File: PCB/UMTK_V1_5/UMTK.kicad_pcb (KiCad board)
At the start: 4 copper layers, 88 parts, among them J1 Motor Out, J2 ESTOP, J3 JST 4pin, J5 PJ-102BH, J8 10033526-N3212LF, Q1 Q_PNP_BEC, U1 DRV8873SPWPRQ1, U10 LM2576HVS-5, U11 SN74LVC1T45DCK, U12 SN74LVC1T45DCK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

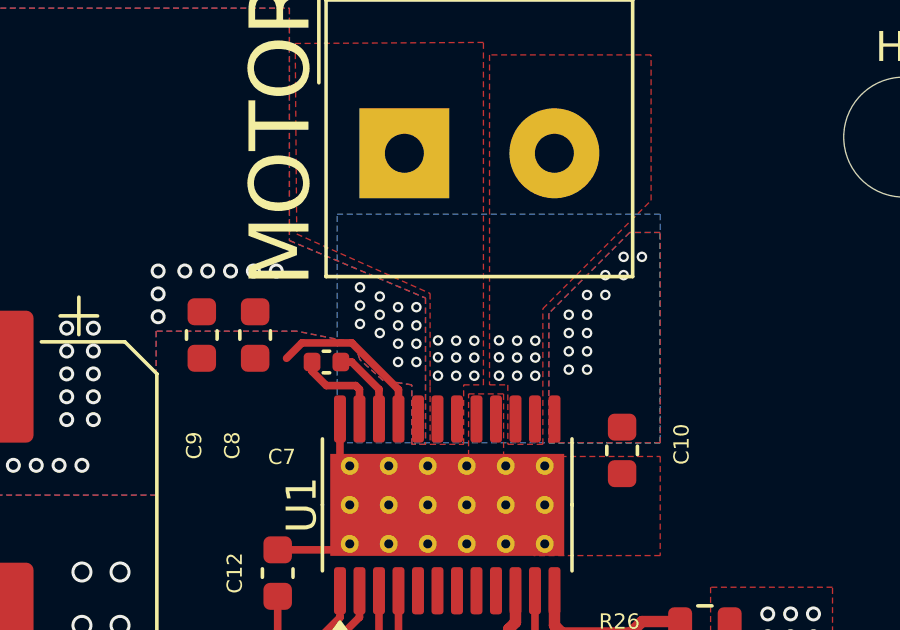
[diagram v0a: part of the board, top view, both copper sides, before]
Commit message: Update Via sizes to 0.3 / 0.45
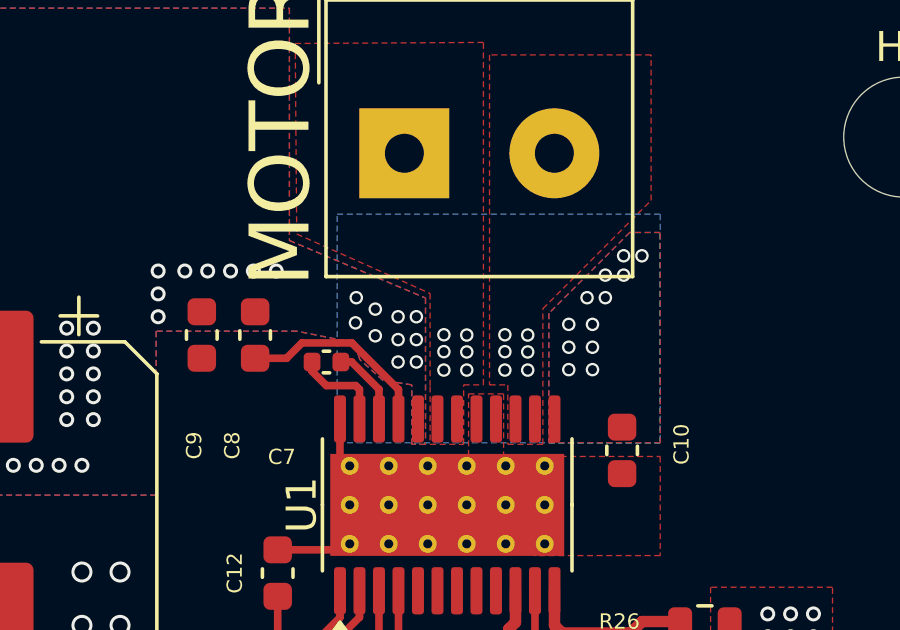
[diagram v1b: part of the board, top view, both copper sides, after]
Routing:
- net Net-(U1-VCP): track 5.57 -> 6.62 mm
- net VMOTOR: vias 80 -> 74
- net /MotorDriver/VM-: vias 9 -> 6
- net /MotorDriver/VM+: vias 9 -> 6

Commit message: Routing
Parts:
- added H9: MountingHole, MountingHole:MountingHole_4mm, F.Cu at (160.0, 25.0)
- J1, J2: footprint TerminalBlock_Altech:Altech_AK100_1x02_P5.00mm -> Connector_Phoenix_MC_HighVoltage:PhoenixContact_MC_1,5_2-G-5.08_1x02_P5.08mm_Horizontal
- J3: value JST 4pin -> LOADCELL; footprint Connector_JST:JST_XH_B4B-XH-A_1x04_P2.50mm_Vertical -> Connector_Phoenix_MC:PhoenixContact_MC_1,5_4-G-3.81_1x04_P3.81mm_Horizontal
- moved J3 8.70 mm to (97.7, 25.9), turned to 180 degrees
- moved J1 8.63 mm to (177.0, 25.6), turned to 180 degrees
- moved H7 5.39 mm to (170.0, 72.0)
- moved H8 5.39 mm to (135.0, 72.0)
- moved J2 4.87 mm to (148.3, 25.5), turned to 180 degrees
- moved JP2 4.45 mm to (121.8, 44.7)
- moved JP3 3.43 mm to (121.8, 49.1)
- moved C10 3.36 mm to (179.0, 35.4)
- moved C7 3.36 mm to (169.1, 32.5)
- moved C8 3.36 mm to (166.7, 31.6)
- moved U1 3.36 mm to (173.1, 37.3)
- moved C12 3.36 mm to (167.5, 39.5)
- moved C9 3.36 mm to (165.0, 31.6)
- moved R26 3.36 mm to (181.7, 41.1)
- moved R27 3.36 mm to (181.7, 43.0)
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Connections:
- J1 pad 1: /MotorDriver/VM+ -> /MotorDriver/VM-
- J1 pad 2: /MotorDriver/VM- -> /MotorDriver/VM+
- J2 pad 1: +12V -> VMOTOR
- J2 pad 2: VMOTOR -> +12V
- J3 pad 2: /HX711/LCS- -> /HX711/LCS+
- J3 pad 3: /HX711/LCS+ -> /HX711/LCS-
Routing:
- net +5V: track 25.6 -> 268.7 mm, vias 22 -> 48
- net /Arduino/MOT_DISABLE: track 0.00 -> 177.6 mm, vias 0 -> 3
- net /Arduino/MOT_nOL: track 0.00 -> 169.8 mm, vias 0 -> 2
- net /Arduino/MOT_nITRIP: track 0.00 -> 169.0 mm, vias 0 -> 2
- net /Arduino/MOT_PH_IN2: track 0.00 -> 164.1 mm, vias 0 -> 4
- net /Arduino/MOT_EN_N1: track 0.00 -> 161.4 mm, vias 0 -> 1
- net /Arduino/MOT_SENSE2: track 5.61 -> 146.8 mm, vias 0 -> 2
- net /Arduino/MOT_SENSE1: track 8.35 -> 134.7 mm, vias 0 -> 2
- net /Arduino/SLIDE_DAT_DIR: track 10.1 -> 123.6 mm, vias 0 -> 2
- net /Arduino/SLIDE_DAT: track 0.00 -> 106.2 mm, vias 0 -> 2
- net /Arduino/SLIDE_CLK_DIR: track 12.3 -> 111.6 mm, vias 0 -> 2
- net /Arduino/SLIDE_CLK: track 0.00 -> 92.8 mm, vias 0 -> 2
- net /Arduino/SW_1: track 10.2 -> 92.2 mm, vias 1 -> 2
- net /Arduino/SW_5: track 66.3 -> 1.90 mm
- net /Arduino/LC_SCK: track 0.00 -> 54.9 mm, vias 0 -> 1
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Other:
- board text added: "3v3 CUT & Solder"
- board text removed: "3v3 (CUT & Solder)"

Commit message: Dumbass has push and shove routing off
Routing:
- net /Arduino/SW_2: track 0.00 -> 97.4 mm, vias 0 -> 4
- net +5V: track 268.7 -> 265.6 mm
- net /Arduino/SW_5: track 1.90 -> 0.00 mm, vias 1 -> 0
- net /Arduino/SW_4: track 1.65 -> 0.00 mm, vias 1 -> 0
- net GND: track 60.3 -> 60.2 mm, vias 175 -> 174
- net Net-(U6-DIG_5): vias 4 -> 2
- net +12V: vias 42 -> 40

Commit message: Routing Done
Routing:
- net /Arduino/MOT_MODE: track 4.63 -> 158.5 mm, vias 0 -> 3
- net /Arduino/SW_5: track 0.00 -> 139.0 mm, vias 0 -> 4
- net /Arduino/SW_4: track 0.00 -> 132.6 mm, vias 0 -> 4
- net /Arduino/SW_3: track 0.00 -> 111.1 mm, vias 0 -> 3
- net /Arduino/LC_RATE: track 0.00 -> 72.9 mm, vias 0 -> 2
- net VDD: track 33.4 -> 82.4 mm, vias 19 -> 23
- net +5V: track 265.6 -> 310.8 mm, vias 48 -> 50
- net /Arduino/MOT_nITRIP: track 169.0 -> 182.8 mm
- net /Arduino/MOT_nOL: track 169.7 -> 183.3 mm
- net Net-(U4-B): track 0.00 -> 12.1 mm
- net GND: track 60.2 -> 70.5 mm, vias 174 -> 230
- net /Arduino/SW_2: track 97.4 -> 105.0 mm
- net /Arduino/SW_1: track 92.2 -> 86.8 mm
- net Net-(D1-K): track 0.00 -> 4.12 mm
- net /Arduino/SLIDE_CLK: track 92.8 -> 90.4 mm
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- added copper zone on B.Cu, net +12V
- added copper zone on In2.Cu, net +12V
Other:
- board outline added: 170 x 80 mm

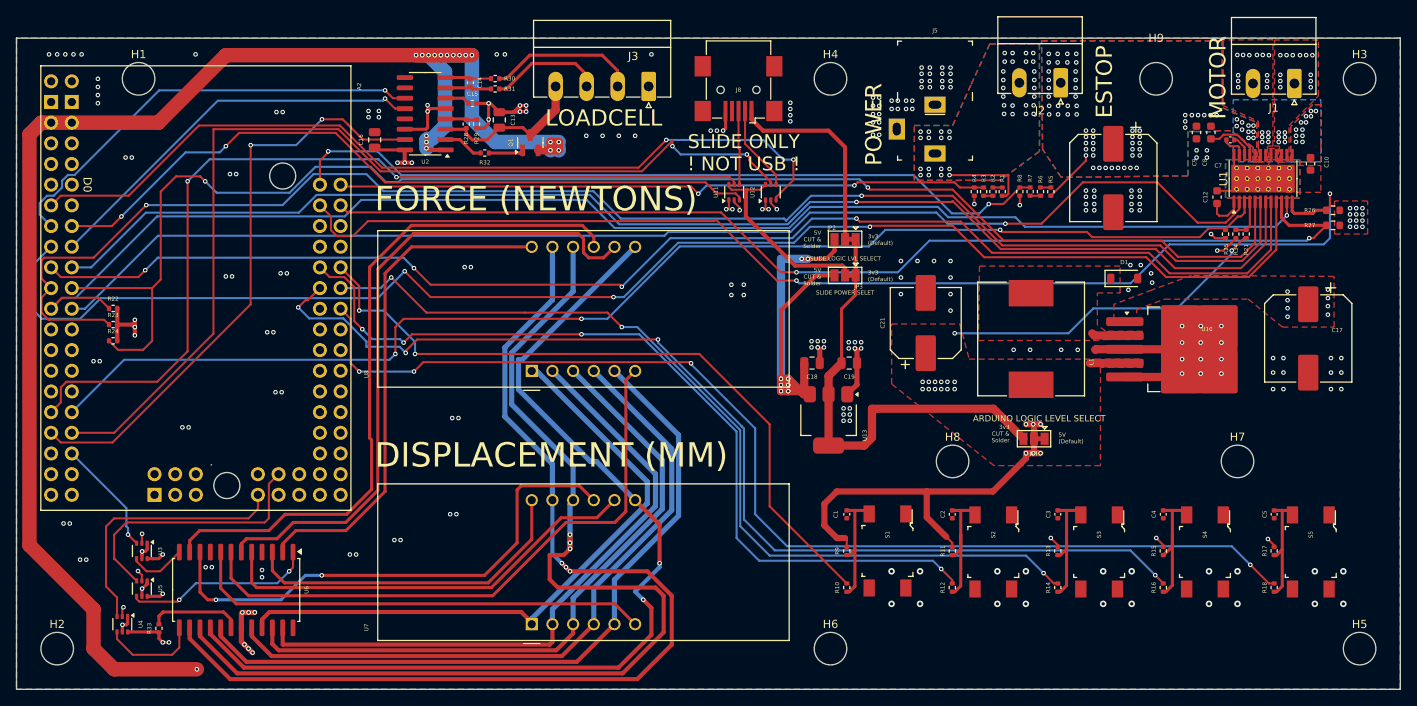
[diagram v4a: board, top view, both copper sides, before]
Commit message: Added Sinkscreen Annotations, PCB Done for now
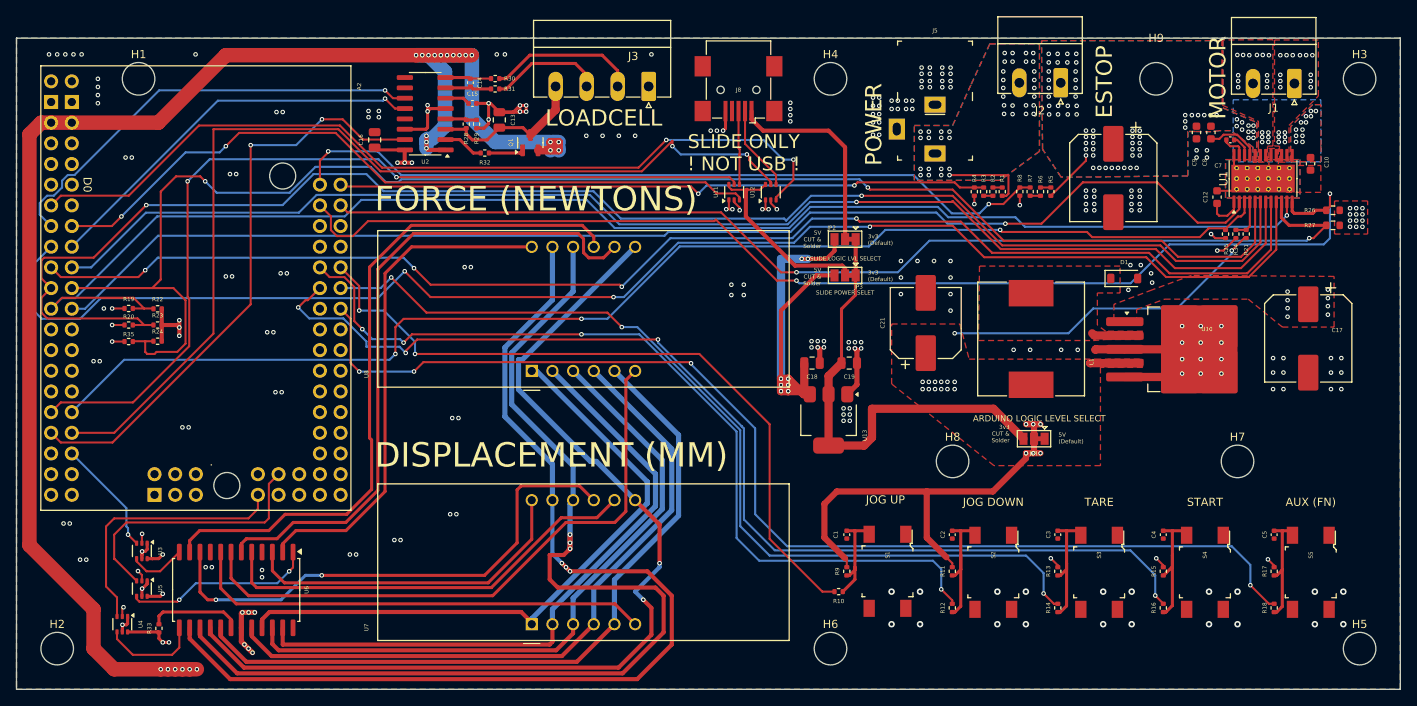
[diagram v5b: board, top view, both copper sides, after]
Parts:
- added R19: DNP, Resistor_SMD:R_0402_1005Metric, F.Cu at (33.8, 53.2)
- added R20: DNP, Resistor_SMD:R_0402_1005Metric, F.Cu at (33.8, 55.2)
- added R35: DNP, Resistor_SMD:R_0402_1005Metric, F.Cu at (33.8, 57.3)
- moved R22 5.46 mm to (37.3, 53.3)
- moved R23 5.46 mm to (37.3, 55.2)
- moved R24 5.46 mm to (37.3, 57.2)
- moved C1 2.50 mm to (122.0, 81.0)
- moved C2 2.50 mm to (135.0, 81.0)
- moved C3 2.50 mm to (147.9, 81.0)
- moved C4 2.50 mm to (160.9, 81.0)
- moved C5 2.50 mm to (174.5, 81.0)
- moved R11 2.50 mm to (135.0, 85.5)
- moved R12 2.50 mm to (135.0, 90.0)
- moved R13 2.50 mm to (147.9, 85.5)
- moved R14 2.50 mm to (147.9, 90.0)
- moved R15 2.50 mm to (160.9, 85.5)
- moved R16 2.50 mm to (160.9, 90.0)
- moved R17 2.50 mm to (174.5, 85.5)
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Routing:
- net /Arduino/MOT_nSLEEP: track 171.3 -> 178.2 mm
- net /Arduino/MOT_nOL: track 183.3 -> 190.2 mm
- net /Arduino/MOT_nITRIP: track 182.8 -> 189.6 mm
- net GND: track 70.5 -> 75.1 mm, vias 230 -> 234
- net VDD: track 82.4 -> 86.8 mm
- net /Arduino/SW_4: track 132.6 -> 135.1 mm
- net /Arduino/SW_2: track 105.0 -> 107.5 mm
- net /Arduino/SW_3: track 111.1 -> 113.6 mm
- net /Arduino/SW_5: track 139.0 -> 141.5 mm
- net Net-(C1-Pad2): track 14.8 -> 12.6 mm
- net /Arduino/SW_1: track 86.8 -> 88.1 mm
- net /Arduino/SLIDE_CLK_DIR: track 111.6 -> 110.4 mm
- net +5V: vias 50 -> 55
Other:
- board text added: "! CONNECT ARDUINO, AND ALL SENSORS ! ! BEFORE APPLYING POWER TO BOARD !"
- board text added: "AUX (FN)"
- board text added: "Design By: Crystal Liu, Michael Ding July 2024"
- board text added: "Digital Readout Slide: Connect to Mini USB Port Default Power Voltage: 3.3V Default Logic Level: 3.3v Voltage Switchable With JP2 and JP3 Cut 3.3V Side And Solder"
- board text added: "JOG DOWN"
- board text added: "JOG UP"
- board text added: "LoadCell: IC: HX711, Channel: A Excitation: ~4.8V Gain: 64x or 128x 20mV FS for 128x"
- board text added: "Microcontroller: Use Arduino Mega Pro Mini (Clone) Default IO Voltage: 5V Switchable to 3.3V By Cutting JP1 and Soldering 3.3V Side"
- board text added: "Motor Driver: TI DRV8873H MAX 10A Peak Desolder R24 For 6.5A Soft Limit"
- board text added: "Power IN: Min 9V MAX 32V"
- board text added: "START"
- board text added: "TARE"
- board text added: "UMTK V1.5"
